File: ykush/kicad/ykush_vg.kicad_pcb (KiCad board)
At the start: 2 copper layers, 89.9 x 54.9 mm, 60 parts, among them J1 USB-C 16P, J2 USB-A port, J3 USB-A port, J4 USB-A port, J5 EXT 5V, SW1 BOOT, U1 FE1.1s, U2 CH552G, U3 SY6280AAC, U4 USBLC6-2SC6, U5 SY6280AAC, U6 USBLC6-2SC6, U7 SY6280AAC, U8 USBLC6-2SC6, Y1 12MHz

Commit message: YKUSH-VG board checkpoint: all nets routed except EN2, 0 DRC errors
Routing: GND routed as a net, EN lines prioritised in the next sweep.

Co-Authored-By: Claude Opus 5.5 <noreply@anthropic.com>
Claude-Session: https://claude.ai/code/session_01EEWbo5vCC8AQXSYmE1aT85
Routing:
- net /GND: track 183.4 -> 276.7 mm, vias 133 -> 154
- net /EN2: track 51.4 -> 0.00 mm, vias 5 -> 0
- net /P2_DM: track 13.2 -> 47.5 mm, vias 0 -> 2
- net /P2_DP: track 12.8 -> 47.0 mm, vias 0 -> 2
- net /+5V_PORT: track 219.6 -> 185.5 mm, vias 27 -> 8
- net /MCU_DM: track 27.5 -> 50.5 mm, vias 2 -> 3
- net /MCU_DP: track 25.8 -> 43.6 mm
- net /VBUS_UP: track 73.5 -> 83.5 mm
- net /+3V3: track 19.9 -> 13.0 mm
- net /VBUS_P3: track 37.5 -> 32.1 mm, vias 1 -> 0
- net /EN3: track 80.7 -> 76.8 mm
- net /EN1: track 32.2 -> 29.8 mm, vias 1 -> 0
- net /VBUS_P1: track 27.0 -> 26.0 mm
- net /P3_DM: track 32.4 -> 33.2 mm
- net /CC1: track 3.63 -> 4.19 mm

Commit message: Port 2: ISET/EN resistors next to their SY6280 pins; EN lines routed earlier
Co-Authored-By: Claude Opus 5.5 <noreply@anthropic.com>
Claude-Session: https://claude.ai/code/session_01EEWbo5vCC8AQXSYmE1aT85
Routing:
- net /GND: track 276.7 -> 143.7 mm, vias 154 -> 144
- net /EN2: track 0.00 -> 52.2 mm, vias 0 -> 2
- net /ISET3: track 4.32 -> 49.8 mm, vias 0 -> 2
- net /MCU_DP: track 43.6 -> 28.3 mm
- net /+3V3: track 13.0 -> 19.7 mm
- net /ISET2: track 5.13 -> 0.00 mm
- net /EN3: track 76.8 -> 81.3 mm
- net /MCU_DM: track 50.5 -> 46.3 mm, vias 3 -> 5
- net /VBUS_UP: track 83.5 -> 79.9 mm, vias 0 -> 1
- net /VBUSM: track 9.20 -> 10.8 mm
- net /VBUS_P1: track 26.0 -> 26.6 mm
- net /P1_DM: track 37.0 -> 37.3 mm, vias 0 -> 3

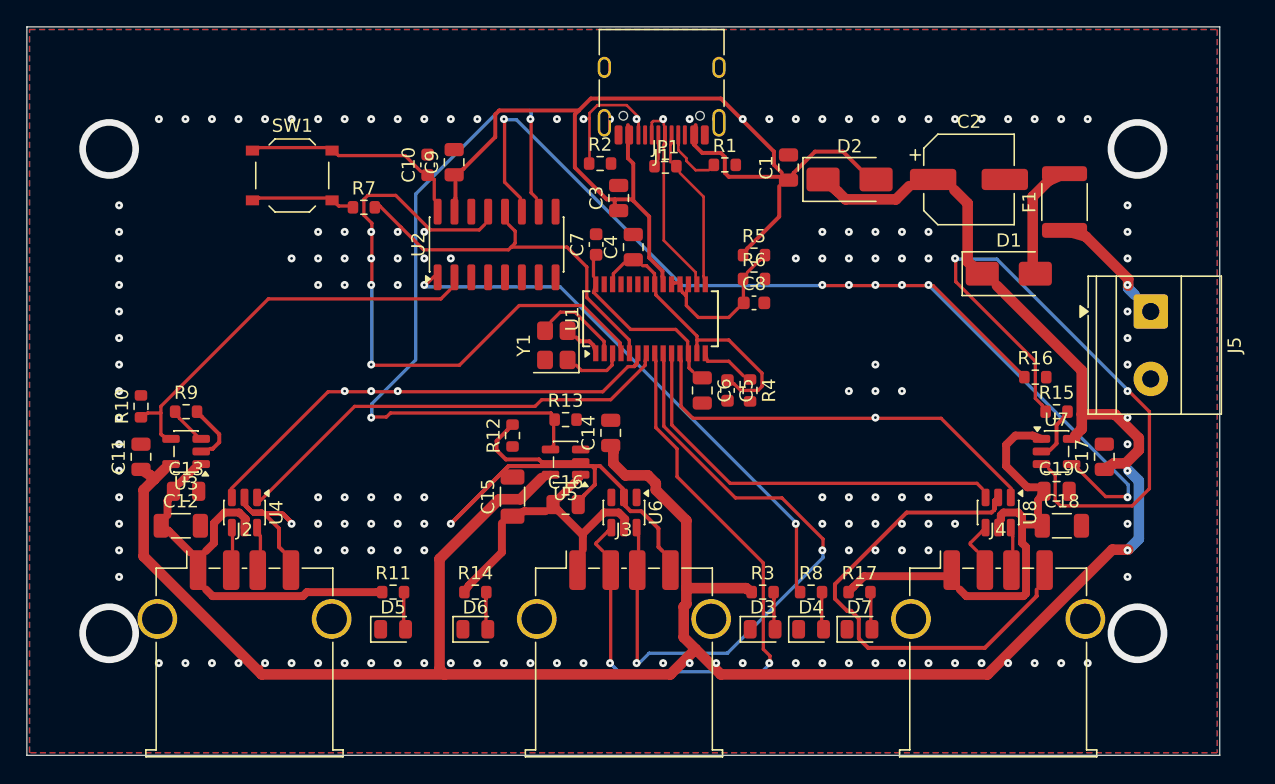
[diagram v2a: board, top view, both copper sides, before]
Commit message: YKUSH-VG: fully routed PCB on Viagrid 9055 (DRC: 0 errors, 0 unconnected, 0 parity) + fab outputs
- kicad/ykush_vg.kicad_pcb: best of a 4-variant routing sweep, all 41 nets routed
- fab/: copper DXFs for LightBurn, Gerbers + drill, holes_to_drill.csv (14 holes),
  positions.csv, top/bottom previews
- README: status, CH552G pin map for the firmware; LAYOUT.md: results and router notes

Co-Authored-By: Claude Opus 5.5 <noreply@anthropic.com>
Claude-Session: https://claude.ai/code/session_01EEWbo5vCC8AQXSYmE1aT85
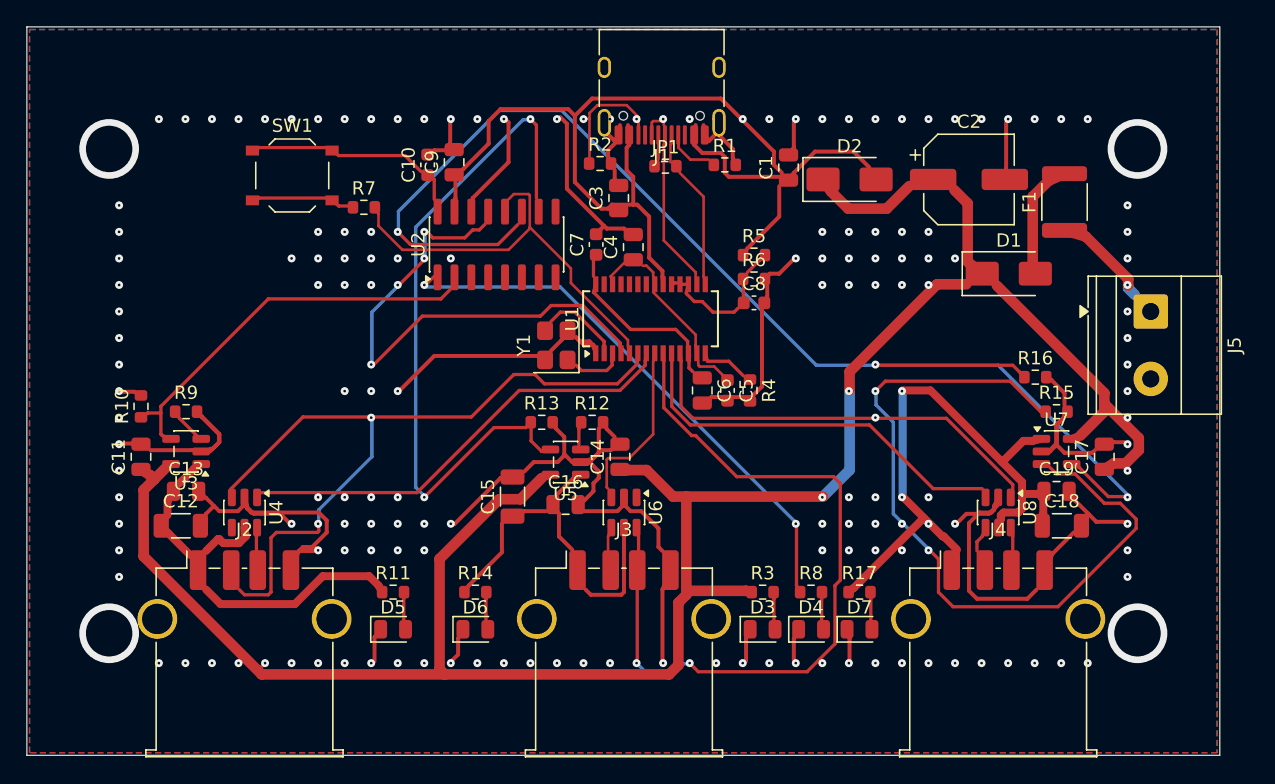
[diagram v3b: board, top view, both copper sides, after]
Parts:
- moved R12 6.08 mm to (146.4, 91.1), turned to 0 degrees
- moved C14 1.93 mm to (148.5, 93.7)
- moved R13 1.81 mm to (142.6, 91.1)
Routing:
- net /GND: track 143.7 -> 219.7 mm
- net /P2_DM: track 47.5 -> 14.3 mm, vias 2 -> 0
- net /P1_DM: track 37.3 -> 57.4 mm, vias 3 -> 2
- net /EN3: track 81.3 -> 98.7 mm, vias 7 -> 3
- net /VBUS_P3: track 32.6 -> 46.8 mm, vias 0 -> 4
- net /+5V_PORT: track 185.2 -> 171.2 mm, vias 8 -> 7
- net /P2_DP: track 47.0 -> 56.2 mm, vias 2 -> 3
- net /ISET3: track 49.8 -> 57.9 mm, vias 2 -> 3
- net /MCU_DM: track 46.3 -> 39.3 mm, vias 5 -> 4
- net /+3V3: track 19.7 -> 12.9 mm
- net /VBUS_P2: track 20.4 -> 23.3 mm
- net /MCU_DP: track 28.3 -> 31.2 mm, vias 1 -> 0
- net /ISET2: track 0.00 -> 1.73 mm
- net /VBUS_UP: track 79.9 -> 81.5 mm
- net /VBUSM: track 10.8 -> 9.39 mm
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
